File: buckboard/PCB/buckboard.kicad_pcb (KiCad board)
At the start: 2 copper layers, 159 parts, among them J1 Conn_01x05, SW1 SW_Push, SW10 SW_Push, SW100_1.25 SW_Push, SW101 SW_Push, SW102 SW_Push, SW103_1.25 SW_Push, SW104_1.25 SW_Push, SW105_1.25 SW_Push, SW106_1.5 SW_Push, SW11 SW_Push, SW12 SW_Push, SW13 SW_Push, SW17 SW_Push, SW18 SW_Push, SW19 SW_Push, SW2 SW_Push, SW20 SW_Push, SW21 SW_Push, SW22 SW_Push, SW23 SW_Push, SW24 SW_Push, SW25 SW_Push, SW26 SW_Push, SW27 SW_Push, SW28 SW_Push, SW29 SW_Push, SW3 SW_Push, SW30_2 SW_Push, SW4 SW_Push, SW5 SW_Push, SW58_1.5 SW_Push, SW59 SW_Push, SW6 SW_Push, SW60 SW_Push, SW61 SW_Push, SW62 SW_Push, SW63 SW_Push, SW64 SW_Push, SW65 SW_Push, SW66 SW_Push, SW67 SW_Push, SW68 SW_Push, SW69 SW_Push, SW7 SW_Push, SW70 SW_Push, SW71 SW_Push, SW71_1.75 SW_Push, SW72 SW_Push, SW73 SW_Push, SW74 SW_Push, SW75 SW_Push, SW76 SW_Push, SW77 SW_Push, SW78 SW_Push, SW79 SW_Push, SW8 SW_Push, SW80 SW_Push, SW81 SW_Push, SW82 SW_Push, SW83 SW_Push, SW84_enter1 SW_Push, SW85_1.25 SW_Push, SW86 SW_Push, SW87 SW_Push, SW88 SW_Push, SW89 SW_Push, SW9 SW_Push, SW90 SW_Push, SW91 SW_Push, SW92 SW_Push, SW93 SW_Push, SW94 SW_Push, SW95 SW_Push, SW96 SW_Push, SW97_2.75 SW_Push, SW98_1.5 SW_Push, SW99_1.25 SW_Push

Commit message: created pcb model and wired it up + added secondary rotary encoder
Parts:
- added SW14: RotaryEncoder, Rotary_Encoder:RotaryEncoder_Alps_EC12E_Vertical_H20mm, F.Cu at (776.1, 90.3)
- A1: moved to F.Cu
- moved J1 72.8 mm to (600.6, 222.8), turned to -82.5 degrees
- moved D108 65.3 mm to (758.0, 95.4), turned to 105 degrees
- moved SW71 65.2 mm to (749.2, 89.6), turned to 15 degrees
- moved SW13 61.6 mm to (730.8, 94.5), turned to 15 degrees
- moved D13 61.5 mm to (739.6, 100.4), turned to 105 degrees
- moved SW12 58.1 mm to (712.4, 99.4), turned to 15 degrees
- moved D12 57.8 mm to (721.2, 105.3), turned to 105 degrees
- moved D30 57.6 mm to (784.4, 120.4), turned to 105 degrees
- moved D106 56.5 mm to (804.2, 194.0), turned to 105 degrees
- moved D84 56.4 mm to (791.8, 148.0), turned to 105 degrees
- moved D97 56.1 mm to (799.2, 175.6), turned to 105 degrees
- moved SW11 54.8 mm to (694.0, 104.4), turned to 15 degrees
- moved D11 54.4 mm to (702.8, 110.2), turned to 105 degrees
- moved SW84_enter1 54.2 mm to (780.7, 142.8), turned to 15 degrees
- moved SW30_2 54.0 mm to (766.4, 117.0), turned to 15 degrees
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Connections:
- net row2 renamed p19
- net row3 renamed p20
- net row4 renamed p21
- net row5 renamed p22
- net row6 renamed p26
- A1 pad 32: unconnected-(A1-GPIO27_ADC1-Pad32) -> EC12A
- A1 pad 34: unconnected-(A1-GPIO28_ADC2-Pad34) -> EC12B
- OLED DISPLAY1 pad 1: SDA -> GND
- OLED DISPLAY1 pad 2: SCL -> +3.3V
- OLED DISPLAY1 pad 3: VCC -> SCL
- OLED DISPLAY1 pad 4: GND -> SDA
- SW1 pad 2: col1 -> col2
- SW10 pad 2: col10 -> col11
- SW11 pad 2: col11 -> col12
- SW12 pad 2: col12 -> col13
- SW13 pad 2: col13 -> col14
- SW2 pad 2: col2 -> col3
- SW3 pad 2: col3 -> col4
- SW4 pad 2: col4 -> col5
- SW5 pad 2: col5 -> col6
- SW6 pad 2: col6 -> col7
- SW7 pad 2: col7 -> col8
- SW8 pad 2: col8 -> col9
- SW9 pad 2: col9 -> col10
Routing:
- net p26: track 0.00 -> 639.9 mm, vias 0 -> 4
- net p22: track 0.00 -> 609.6 mm, vias 0 -> 2
- net p19: track 0.00 -> 576.0 mm, vias 0 -> 3
- net p21: track 0.00 -> 570.7 mm, vias 0 -> 5
- net p20: track 0.00 -> 554.2 mm, vias 0 -> 4
- net row1: track 0.00 -> 464.3 mm
- net col14: track 0.00 -> 344.6 mm, vias 0 -> 2
- net col13: track 0.00 -> 288.8 mm, vias 0 -> 2
- net col12: track 0.00 -> 282.6 mm, vias 0 -> 2
- net EC11SWB: track 0.00 -> 256.5 mm
- net col11: track 0.00 -> 253.2 mm, vias 0 -> 2
- net col2: track 0.00 -> 245.7 mm
- net col3: track 0.00 -> 230.5 mm
- net col10: track 0.00 -> 219.1 mm, vias 0 -> 1
- net col7: track 0.00 -> 209.5 mm
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- added copper zone on B.Cu, net GND
- added copper zone on F.Cu, net GND
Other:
- board outline added: 387.6 x 194.6 mm

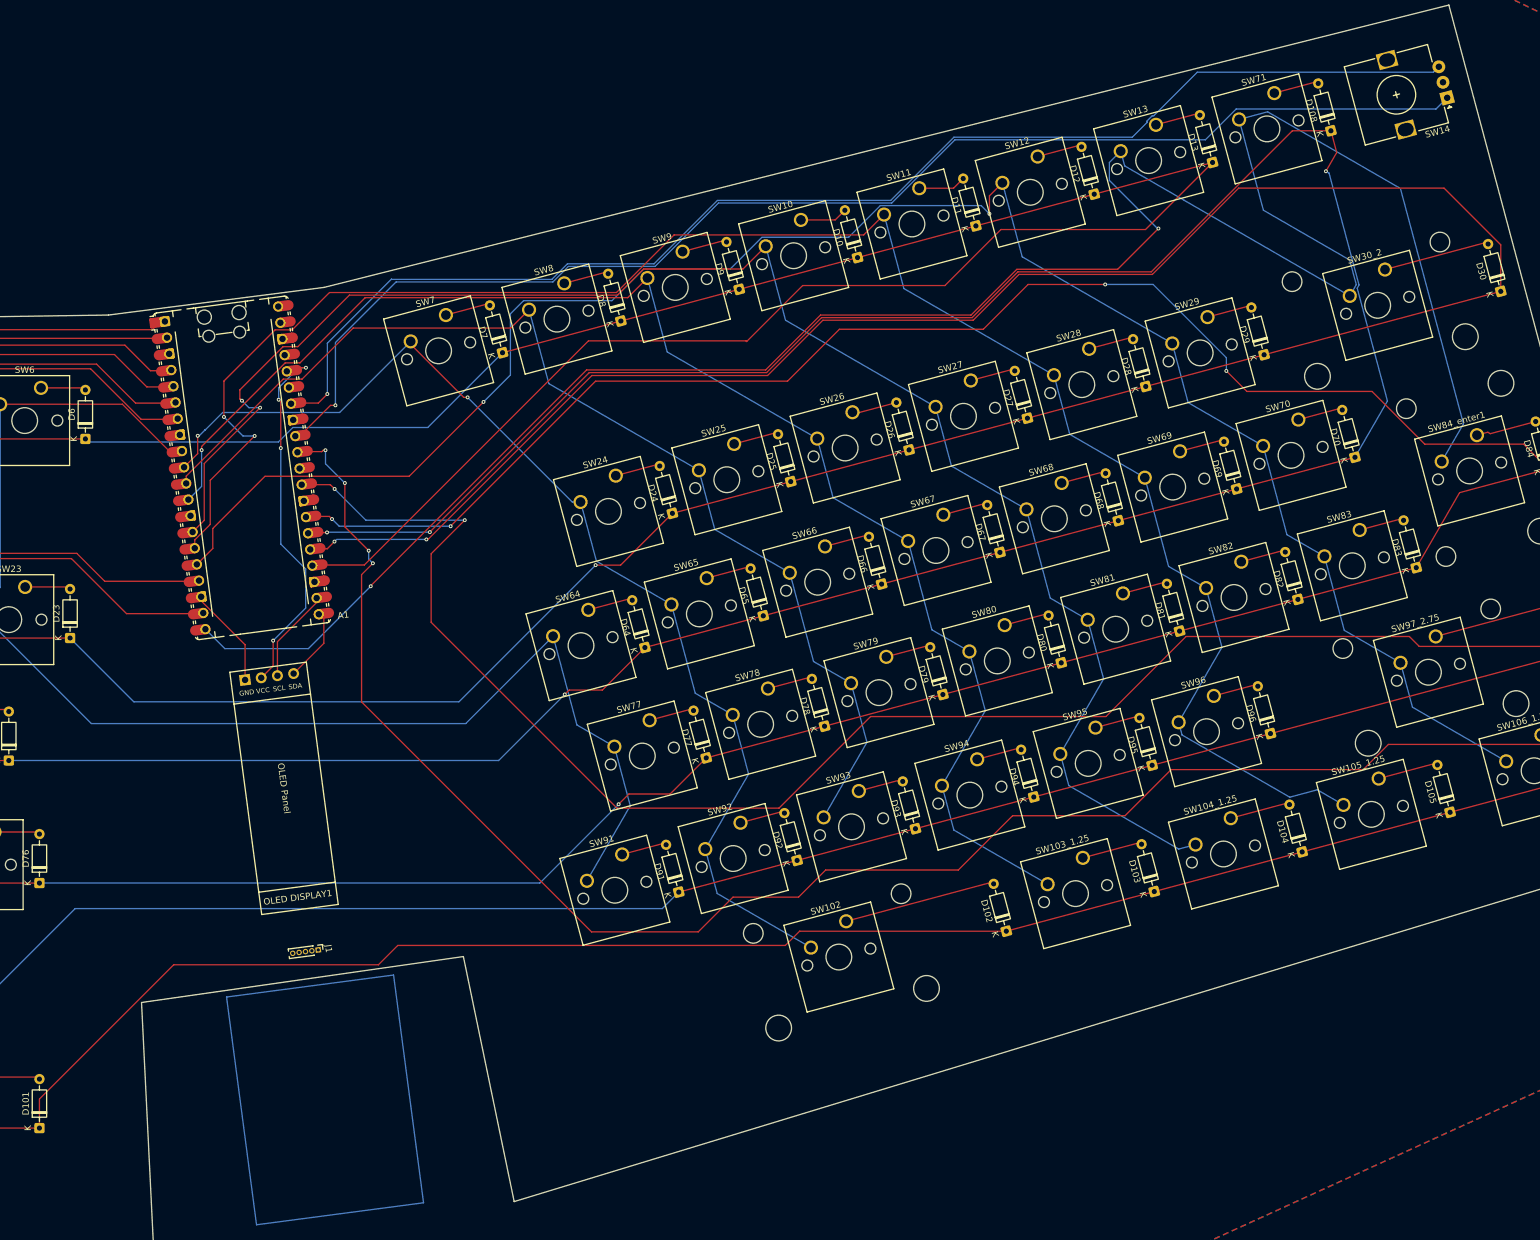
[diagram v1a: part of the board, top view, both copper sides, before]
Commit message: updated pcb to have joystick module support (- 1 rotary encoder)+ gerber
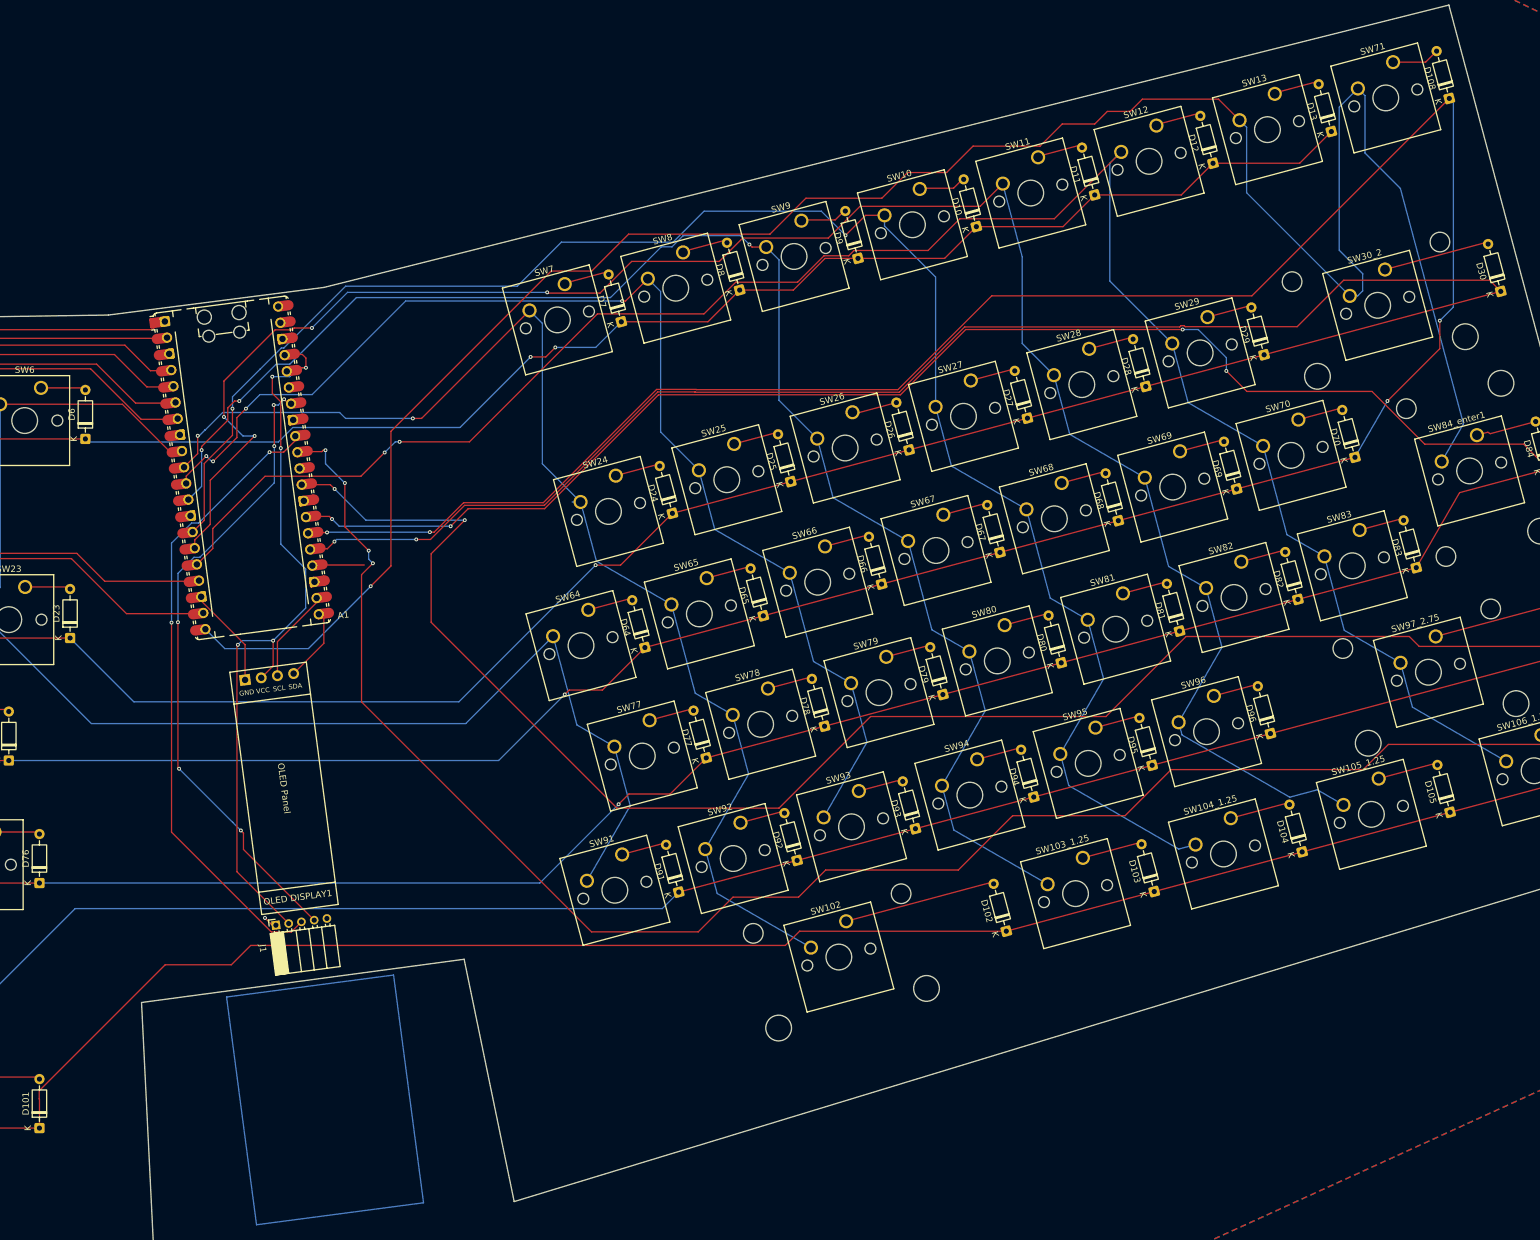
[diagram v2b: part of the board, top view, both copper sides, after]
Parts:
- removed SW14: RotaryEncoder, Rotary_Encoder:RotaryEncoder_Alps_EC12E_Vertical_H20mm
- J1: footprint Connector_PinHeader_1.00mm:PinHeader_1x05_P1.00mm_Vertical -> Connector_PinSocket_2.00mm:PinSocket_1x05_P2.00mm_Horizontal
- moved D10 19.1 mm to (702.9, 110.3)
- moved D9 19.1 mm to (684.5, 115.3)
- moved SW11 19.1 mm to (712.5, 99.6)
- moved SW12 19.1 mm to (730.9, 94.6)
- moved SW8 19.1 mm to (657.3, 114.3)
- moved SW9 19.1 mm to (675.7, 109.4)
- moved D11 19.1 mm to (721.3, 105.4)
- moved D12 19.1 mm to (739.7, 100.5)
- moved D13 19.1 mm to (758.1, 95.6)
- moved D7 19.1 mm to (647.7, 125.1)
- moved D8 19.1 mm to (666.1, 120.2)
- moved SW10 19.1 mm to (694.1, 104.5)
- moved SW13 19.1 mm to (749.3, 89.7)
- moved SW7 19.1 mm to (638.9, 119.3)
- moved SW71 19.1 mm to (767.7, 84.8)
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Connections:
- A1 pad 24: row1 -> p18
- A1 pad 32: EC12A -> VRx
- A1 pad 34: EC12B -> VRy
- J1 pad 5: JSW -> (no net)
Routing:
- net EC12A: track 205.8 -> 0.00 mm, vias 1 -> 0
- net EC12B: track 204.1 -> 0.00 mm, vias 1 -> 0
- net row1: track 464.3 -> 328.2 mm, vias 0 -> 2
- net VRy: track 0.00 -> 99.8 mm, vias 0 -> 6
- net VRx: track 0.00 -> 99.2 mm, vias 0 -> 2
- net +3.3V: track 57.6 -> 116.7 mm, vias 4 -> 5
- net p20: track 554.2 -> 582.1 mm, vias 4 -> 5
- net col8: track 173.1 -> 191.7 mm
- net col10: track 219.1 -> 236.4 mm, vias 1 -> 3
- net col9: track 171.0 -> 188.2 mm, vias 0 -> 4
- net p19: track 576.0 -> 560.1 mm
- net col11: track 253.2 -> 267.4 mm
- net col12: track 282.6 -> 296.7 mm, vias 2 -> 4
- net col13: track 288.8 -> 296.7 mm
- net p18: track 0.00 -> 6.98 mm
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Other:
- outline, holes or cut-outs redrawn

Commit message: added firmware to the repo (still not working)
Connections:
- A1 pad 37: +3.3V -> JSW
- J1 pad 5: (no net) -> JSW
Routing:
- net +3.3V: track 116.7 -> 109.6 mm, vias 5 -> 4
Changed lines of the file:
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@@
 		)
 		(fp_line
-			(start -1.209997 2.36)
+			(start -1.209996 2.36)
 			(end -0.862918 2.359999)
 			(stroke
@@
 			(layers "*.Cu" "*.Mask")
 			(remove_unused_layers no)
+			(net "JSW")
 			(pinfunction "Pin_5_5")
 			(pintype "passive")
@@
 			(layers "*.Cu" "*.Mask")
 			(remove_unused_layers no)
-			(net "+3.3V")
+			(net "JSW")
 			(pinfunction "3V3_EN_37")
 			(pintype "passive")
@@
 			(layers "F.Cu" "F.Mask")
 			(roundrect_rratio 0.5)
-			(net "+3.3V")
+			(net "JSW")
 			(pinfunction "3V3_EN_37")
 			(pintype "passive")
@@
 	)
 	(segment
-		(start 596.737342 179.833341)
-		(end 601.440271 175.130412)
-		(width 0.2)
-		(layer "F.Cu")
-		(net "SDA")
-	)
-	(segment
-		(start 601.440271 175.130412)
-		(end 601.440271 170.507199)
-		(width 0.2)
-		(layer "F.Cu")
-		(net "SDA")
-	)
-	(segment
-		(start 594.219072 174.878591)
-		(end 594.219072 180.164877)
-		(width 0.2)
-		(layer "F.Cu")
-		(net "SCL")
-	)
-	(segment
-		(start 601.108734 167.988929)
-		(end 594.219072 174.878591)
-		(width 0.2)
-		(layer "F.Cu")
-		(net "SCL")
-	)
-	(segment
 		(start 582.356152 168.519972)
 		(end 582.356152 167.895835)
@@
 	)
 	(segment
+		(start 591.700802 180.496414)
+		(end 593.55 178.647216)
+		(width 0.2)
+		(layer "F.Cu")
+		(net "+3.3V")
+	)
+	(segment
+		(start 593.42 133.67)
+		(end 593.42 136.26)
+		(width 0.2)
+		(layer "F.Cu")
+		(net "+3.3V")
+	)
+	(segment
+		(start 587.928857 175.501143)
+		(end 588.07 175.36)
+		(width 0.2)
+		(layer "F.Cu")
+		(net "+3.3V")
+	)
+	(segment
+		(start 595.967111 218.701053)
+		(end 587.928857 210.662799)
+		(width 0.2)
+		(layer "F.Cu")
+		(net "+3.3V")
+	)
+	(segment
+		(start 594.74 137.58)
+		(end 594.74 144.78)
+		(width 0.2)
+		(layer "F.Cu")
+		(net "+3.3V")
+	)
+	(segment
+		(start 593.55 178.647216)
+		(end 593.55 174.71)
+		(width 0.2)
+		(layer "F.Cu")
+		(net "+3.3V")
+	)
+	(segment
+		(start 593.42 136.26)
+		(end 594.74 137.58)
+		(width 0.2)
+		(layer "F.Cu")
+		(net "+3.3V")
+	)
+	(segment
+		(start 587.928857 210.662799)
+		(end 587.928857 175.501143)
+		(width 0.2)
+		(layer "F.Cu")
+		(net "+3.3V")
+	)
+	(segment
+		(start 596.920372 132.28)
+		(end 596.467223 132.733149)
+		(width 0.2)
+		(layer "F.Cu")
+		(net "+3.3V")
+	)
+	(via
+		(at 588.07 175.36)
+		(size 0.6)
+		(drill 0.3)
+		(layers "F.Cu" "B.Cu")
+		(net "+3.3V")
+	)
+	(via
+		(at 594.74 144.78)
+		(size 0.6)
+		(drill 0.3)
+		(layers "F.Cu" "B.Cu")
+		(net "+3.3V")
+	)
+	(via
+		(at 593.55 174.71)
+		(size 0.6)
+		(drill 0.3)
+		(layers "F.Cu" "B.Cu")
+		(net "+3.3V")
+	)
+	(via
+		(at 593.42 133.67)
+		(size 0.6)
+		(drill 0.3)
+		(layers "F.Cu" "B.Cu")
+		(net "+3.3V")
+	)
+	(segment
+		(start 598.608247 163.568187)
+		(end 594.74 159.69994)
+		(width 0.2)
+		(layer "B.Cu")
+		(net "+3.3V")
+	)
+	(segment
+		(start 596.135808 133.67)
+		(end 597.525808 132.28)
+		(width 0.2)
+		(layer "B.Cu")
+		(net "+3.3V")
+	)
+	(segment
+		(start 594.74 159.69994)
+		(end 594.74 144.78)
+		(width 0.2)
+		(layer "B.Cu")
+		(net "+3.3V")
+	)
+	(segment
+		(start 588.07 175.36)
+		(end 588.72 174.71)
+		(width 0.2)
+		(layer "B.Cu")
+		(net "+3.3V")
+	)
+	(segment
+		(start 598.608247 169.651753)
+		(end 598.608247 163.568187)
+		(width 0.2)
+		(layer "B.Cu")
+		(net "+3.3V")
+	)
+	(segment
+		(start 593.42 133.67)
+		(end 596.135808 133.67)
+		(width 0.2)
+		(layer "B.Cu")
+		(net "+3.3V")
+	)
+	(segment
+		(start 593.55 174.71)
+		(end 598.608247 169.651753)
+		(width 0.2)
+		(layer "B.Cu")
+		(net "+3.3V")
+	)
+	(segment
+		(start 588.72 174.71)
+		(end 593.55 174.71)
+		(width 0.2)
+		(layer "B.Cu")
+		(net "+3.3V")
+	)
+	(segment
+		(start 596.737342 179.833341)
+		(end 601.440271 175.130412)
+		(width 0.2)
+		(layer "F.Cu")
+		(net "SDA")
+	)
+	(segment
+		(start 601.440271 175.130412)
+		(end 601.440271 170.507199)
+		(width 0.2)
+		(layer "F.Cu")
+		(net "SDA")
+	)
+	(segment
+		(start 594.219072 174.878591)
+		(end 594.219072 180.164877)
+		(width 0.2)
+		(layer "F.Cu")
+		(net "SCL")
+	)
+	(segment
+		(start 601.108734 167.988929)
+		(end 594.219072 174.878591)
+		(width 0.2)
+		(layer "F.Cu")
+		(net "SCL")
+	)
+	(segment
 		(start 719.455739 208.488095)
 		(end 728.196162 206.146105)
@@
 	)
 	(segment
-		(start 591.700802 180.496414)
-		(end 593.55 178.647216)
-		(width 0.2)
-		(layer "F.Cu")
-		(net "+3.3V")
-	)
-	(segment
-		(start 598.65 132.28)
-		(end 596.920372 132.28)
-		(width 0.2)
-		(layer "F.Cu")
-		(net "+3.3V")
-	)
-	(segment
-		(start 593.42 133.67)
-		(end 593.42 136.26)
-		(width 0.2)
-		(layer "F.Cu")
-		(net "+3.3V")
-	)
-	(segment
-		(start 598.65 130.77)
-		(end 598.65 132.28)
-		(width 0.2)
-		(layer "F.Cu")
-		(net "+3.3V")
-	)
-	(segment
-		(start 587.928857 175.501143)
-		(end 588.07 175.36)
-		(width 0.2)
-		(layer "F.Cu")
-		(net "+3.3V")
-	)
-	(segment
-		(start 595.967111 218.701053)
-		(end 587.928857 210.662799)
-		(width 0.2)
-		(layer "F.Cu")
-		(net "+3.3V")
-	)
-	(segment
-		(start 594.74 137.58)
-		(end 594.74 144.78)
-		(width 0.2)
-		(layer "F.Cu")
-		(net "+3.3V")
-	)
-	(segment
-		(start 593.55 178.647216)
-		(end 593.55 174.71)
-		(width 0.2)
-		(layer "F.Cu")
-		(net "+3.3V")
-	)
-	(segment
-		(start 593.42 136.26)
-		(end 594.74 137.58)
-		(width 0.2)
-		(layer "F.Cu")
-		(net "+3.3V")
-	)
-	(segment
-		(start 587.928857 210.662799)
-		(end 587.928857 175.501143)
-		(width 0.2)
-		(layer "F.Cu")
-		(net "+3.3V")
-	)
-	(segment
-		(start 596.920372 132.28)
-		(end 596.467223 132.733149)
-		(width 0.2)
-		(layer "F.Cu")
-		(net "+3.3V")
-	)
-	(segment
-		(start 596.135686 130.21488)
-		(end 598.09488 130.21488)
-		(width 0.2)
-		(layer "F.Cu")
-		(net "+3.3V")
-	)
-	(segment
-		(start 598.09488 130.21488)
-		(end 598.65 130.77)
-		(width 0.2)
-		(layer "F.Cu")
-		(net "+3.3V")
-	)
-	(via
-		(at 588.07 175.36)
-		(size 0.6)
-		(drill 0.3)
-		(layers "F.Cu" "B.Cu")
-		(net "+3.3V")
-	)
-	(via
-		(at 594.74 144.78)
-		(size 0.6)
-		(drill 0.3)
-		(layers "F.Cu" "B.Cu")
-		(net "+3.3V")
-	)
-	(via
-		(at 598.65 132.28)
-		(size 0.6)
-		(drill 0.3)
-		(layers "F.Cu" "B.Cu")
-		(net "+3.3V")
-	)
-	(via
-		(at 593.55 174.71)
-		(size 0.6)
-		(drill 0.3)
-		(layers "F.Cu" "B.Cu")
-		(net "+3.3V")
-	)
-	(via
-		(at 593.42 133.67)
-		(size 0.6)
-		(drill 0.3)
-		(layers "F.Cu" "B.Cu")
-		(net "+3.3V")
-	)
-	(segment
-		(start 598.608247 163.568187)
-		(end 594.74 159.69994)
-		(width 0.2)
-		(layer "B.Cu")
-		(net "+3.3V")
-	)
-	(segment
-		(start 596.135808 133.67)
-		(end 597.525808 132.28)
-		(width 0.2)
-		(layer "B.Cu")
-		(net "+3.3V")
-	)
-	(segment
-		(start 594.74 159.69994)
-		(end 594.74 144.78)
-		(width 0.2)
-		(layer "B.Cu")
-		(net "+3.3V")
-	)
-	(segment
-		(start 588.07 175.36)
-		(end 588.72 174.71)
-		(width 0.2)
-		(layer "B.Cu")
-		(net "+3.3V")
-	)
-	(segment
-		(start 597.525808 132.28)
-		(end 598.65 132.28)
-		(width 0.2)
-		(layer "B.Cu")
-		(net "+3.3V")
-	)
-	(segment
-		(start 598.608247 169.651753)
-		(end 598.608247 163.568187)
-		(width 0.2)
-		(layer "B.Cu")
-		(net "+3.3V")
-	)
-	(segment
-		(start 593.42 133.67)
-		(end 596.135808 133.67)
-		(width 0.2)
-		(layer "B.Cu")
-		(net "+3.3V")
-	)
-	(segment
-		(start 593.55 174.71)
-		(end 598.608247 169.651753)
-		(width 0.2)
-		(layer "B.Cu")
-		(net "+3.3V")
-	)
-	(segment
-		(start 588.72 174.71)
-		(end 593.55 174.71)
-		(width 0.2)
-		(layer "B.Cu")
-		(net "+3.3V")
-	)
-	(segment
